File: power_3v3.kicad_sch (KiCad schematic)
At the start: 14 parts, among them U5 LTC3111EDE

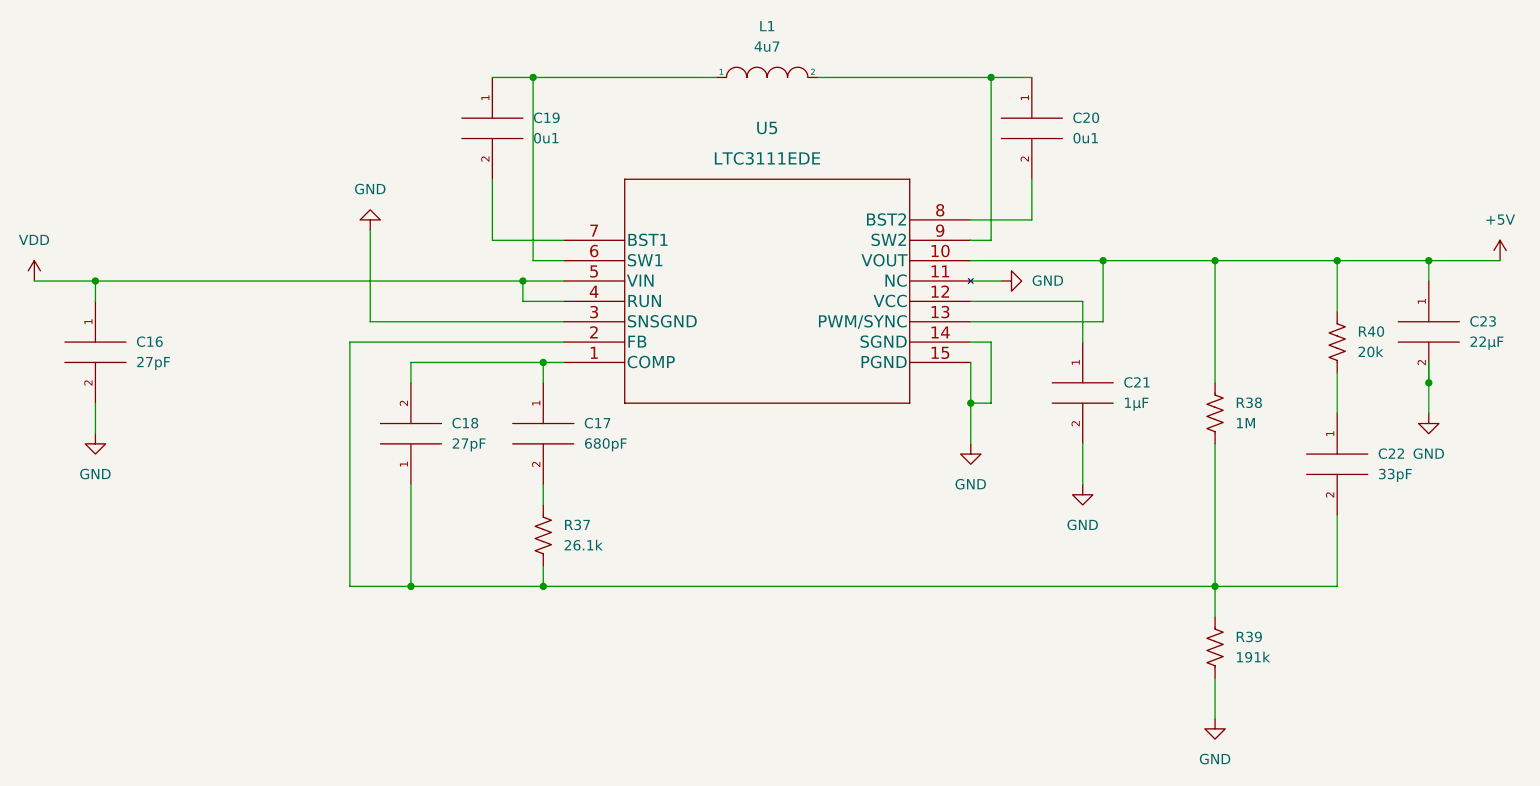
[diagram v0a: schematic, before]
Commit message: Update board design
5v and 3v3 power blocks wired up.
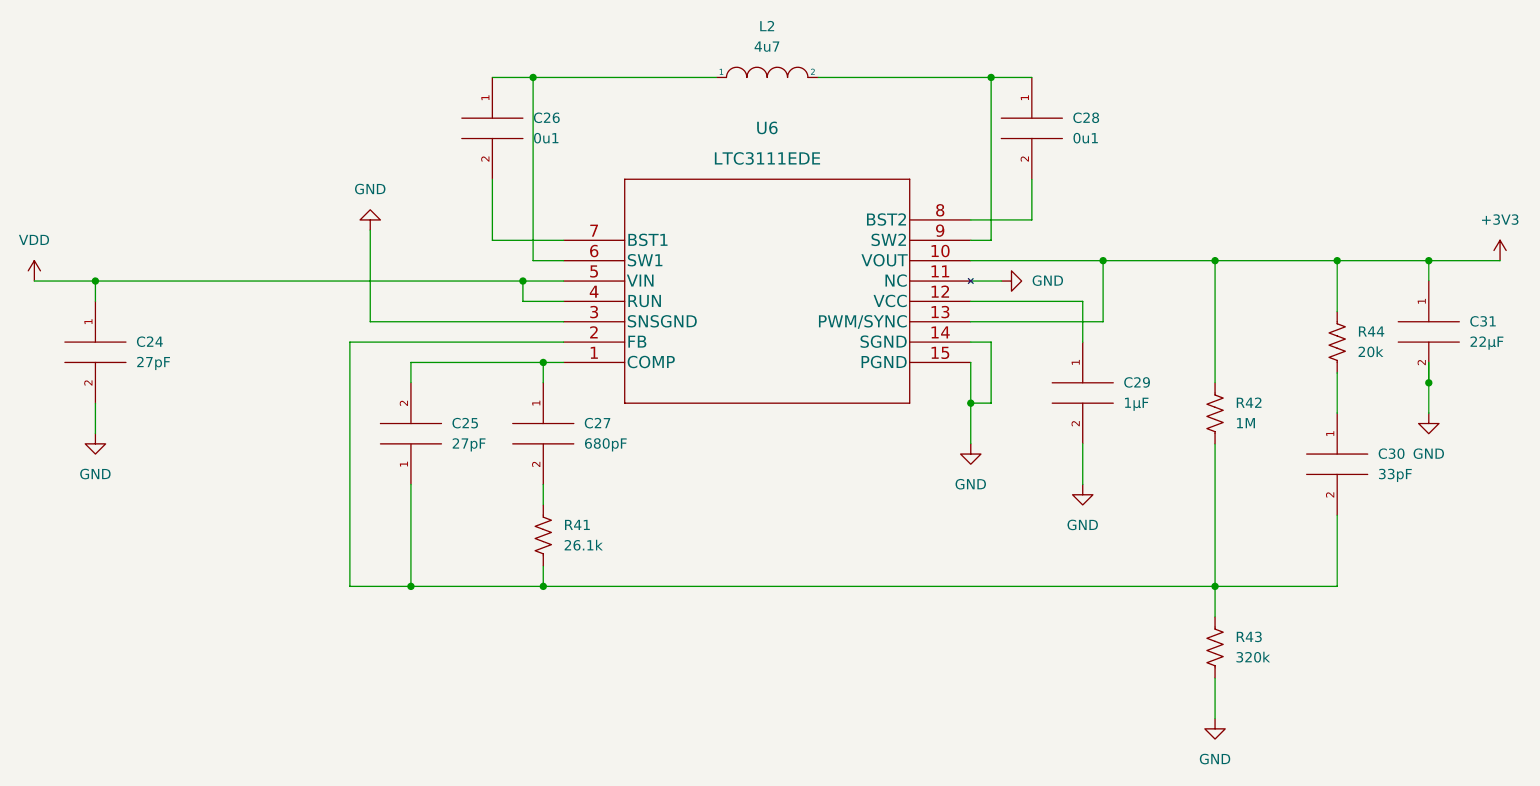
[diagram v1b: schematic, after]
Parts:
- removed C16, C18: 27pF, Capacitor_SMD:C_0201_0603Metric, symbol pspice:C
- removed C17: 680pF, Capacitor_SMD:C_0603_1608Metric, symbol pspice:C
- removed C19, C20: 0u1, Capacitor_SMD:C_0201_0603Metric, symbol pspice:C
- removed C21: 1µF, Capacitor_SMD:C_0201_0603Metric, symbol pspice:C
- removed C22: 33pF, Capacitor_SMD:C_0603_1608Metric, symbol pspice:C
- removed C23: 22µF, Capacitor_SMD:C_1206_3216Metric, symbol pspice:C
- removed L1: 4u7, Inductor_SMD:L_6.3x6.3_H3, symbol pspice:INDUCTOR
- removed R37: 26.1k, Resistor_SMD:R_0201_0603Metric, symbol Device:R_US
- removed R38: 1M, Resistor_SMD:R_0201_0603Metric, symbol Device:R_US
- removed R39: 191k, Resistor_SMD:R_0201_0603Metric, symbol Device:R_US
- removed R40: 20k, Resistor_SMD:R_0201_0603Metric, symbol Device:R_US
- removed U5: LTC3111EDE, Custom:LTC3111EDE-TRPBF, symbol BuckBoost1:LTC3111EDE-PBF
- added C24, C25: 27pF, Capacitor_SMD:C_0201_0603Metric, symbol pspice:C
- added C26, C28: 0u1, Capacitor_SMD:C_0201_0603Metric, symbol pspice:C
- added C27: 680pF, Capacitor_SMD:C_0603_1608Metric, symbol pspice:C
- added C29: 1µF, Capacitor_SMD:C_0201_0603Metric, symbol pspice:C
- added C30: 33pF, Capacitor_SMD:C_0603_1608Metric, symbol pspice:C
- added C31: 22µF, Capacitor_SMD:C_1206_3216Metric, symbol pspice:C
- added L2: 4u7, Inductor_SMD:L_6.3x6.3_H3, symbol pspice:INDUCTOR
- added R41: 26.1k, Resistor_SMD:R_0201_0603Metric, symbol Device:R_US
- added R42: 1M, Resistor_SMD:R_0201_0603Metric, symbol Device:R_US
- added R43: 320k, Resistor_SMD:R_0201_0603Metric, symbol Device:R_US
- added R44: 20k, Resistor_SMD:R_0201_0603Metric, symbol Device:R_US
- added U6: LTC3111EDE, Custom:LTC3111EDE-TRPBF, symbol BuckBoost1:LTC3111EDE-PBF
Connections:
- net GND: now also C24.2, C29.2, C31.2, R43.2, U6.11 (NC), U6.14 (SGND), U6.15 (PGND), U6.3 (SNSGND)
- net VDD: now also C24.1, U6.4 (RUN), U6.5 (VIN)
- new net: C25.2, C27.1, U6.1 (COMP)
- new net: C27.2, R41.1
- new net: C26.1, L2.1, U6.6 (SW1)
- new net: C26.2, U6.7 (BST1)
- new net: C30.1, R44.2
- new net: C29.1, U6.12 (VCC)
- new net: C25.1, C30.2, R41.2, R42.2, R43.1, U6.2 (FB)
- new net: C28.2, U6.8 (BST2)
- new net: C28.1, L2.2, U6.9 (SW2)
- new net +3V3: C31.1, R42.1, R44.1, U6.10 (VOUT), U6.13 (PWM/SYNC)

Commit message: First week after winter break. Changed Power circuit design to use different DC to DC converter Setting correct footprints for the components like resistors and capacitors.
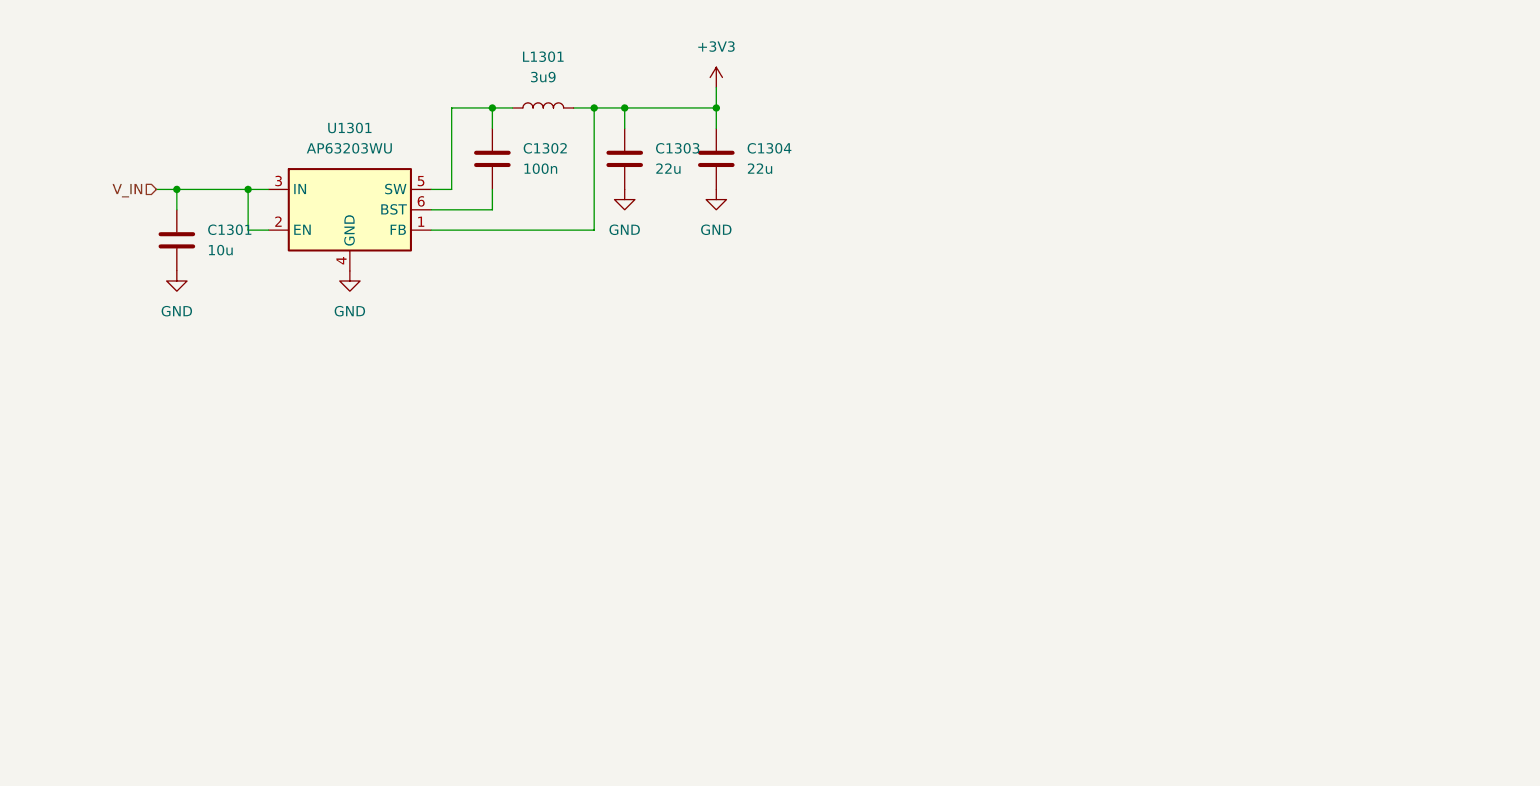
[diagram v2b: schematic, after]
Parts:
- removed C24, C25: 27pF, Capacitor_SMD:C_0201_0603Metric, symbol pspice:C
- removed C26, C28: 0u1, Capacitor_SMD:C_0201_0603Metric, symbol pspice:C
- removed C27: 680pF, Capacitor_SMD:C_0603_1608Metric, symbol pspice:C
- removed C29: 1µF, Capacitor_SMD:C_0201_0603Metric, symbol pspice:C
- removed C30: 33pF, Capacitor_SMD:C_0603_1608Metric, symbol pspice:C
- removed C31: 22µF, Capacitor_SMD:C_1206_3216Metric, symbol pspice:C
- removed L2: 4u7, Inductor_SMD:L_6.3x6.3_H3, symbol pspice:INDUCTOR
- removed R41: 26.1k, Resistor_SMD:R_0201_0603Metric, symbol Device:R_US
- removed R42: 1M, Resistor_SMD:R_0201_0603Metric, symbol Device:R_US
- removed R43: 320k, Resistor_SMD:R_0201_0603Metric, symbol Device:R_US
- removed R44: 20k, Resistor_SMD:R_0201_0603Metric, symbol Device:R_US
- removed U6: LTC3111EDE, Custom:LTC3111EDE-TRPBF, symbol BuckBoost1:LTC3111EDE-PBF
- added C1301: 10u, Capacitor_SMD:C_0603_1608Metric, symbol Device:C
- added C1302: 100n, Capacitor_SMD:C_0805_2012Metric, symbol Device:C
- added C1303, C1304: 22u, Capacitor_SMD:C_0603_1608Metric, symbol Device:C
- added L1301: 3u9, symbol Device:L
- added U1301: AP63203WU, Package_TO_SOT_SMD:TSOT-23-6, symbol Regulator_Switching:AP63203WU
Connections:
- net +3V3: now also C1303.1, C1304.1, L1301.2, U1301.1 (FB)
- net GND: now also C1301.2, C1303.2, C1304.2, U1301.4 (GND)
- new net: C1302.1, L1301.1, U1301.5 (SW)
- new net: C1302.2, U1301.6 (BST)
- new net V_IN: C1301.1, U1301.2 (EN), U1301.3 (IN)

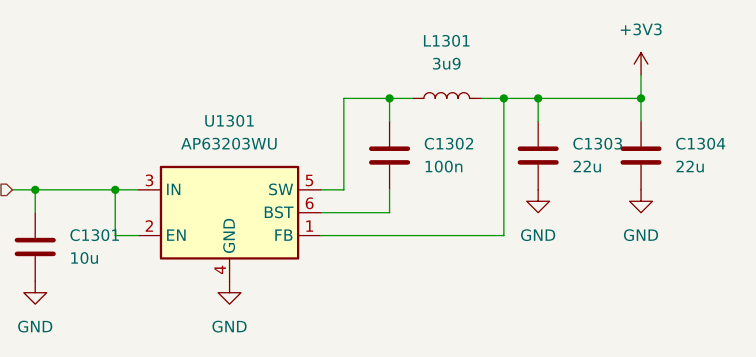
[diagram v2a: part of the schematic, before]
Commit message: Weekend progress
Things that remain:
4 LEDs to Microcontroller
7-Seg to Microcontroller
LCD to Microcontroller
Microphone and Speakers to Microcontroller
Power circuitry
USB-C connector
Reset and Boot buttons
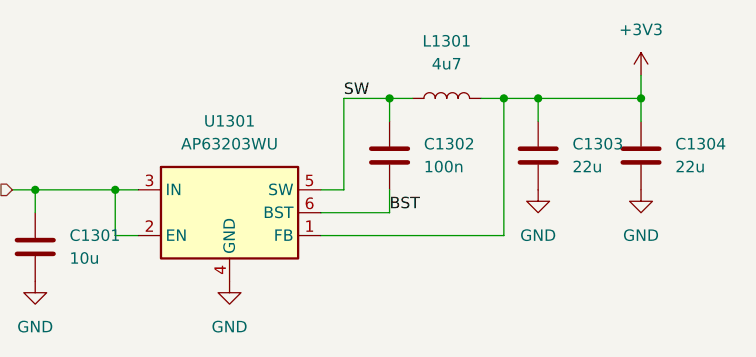
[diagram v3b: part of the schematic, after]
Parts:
- L1301: value 3u9 -> 4u7; footprint (none) -> Inductor_SMD:L_1008_2520Metric; Manufacturer_Name (none) -> Samsung Electro-Mechanics; Manufacturer_Part_Number (none) -> CIGW252010GL4R7MNE
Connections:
- net SW: now reaches C1302.1, L1301.1, U1301.5 (SW)
- net BST: now reaches C1302.2, U1301.6 (BST)
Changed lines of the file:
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@@
     (stroke (width 0) (type default) (color 0 0 0 0))
+  )
+  (label "SW" (at 109.22 58.42 0)
+    (effects (font (size 1.27 1.27)) (justify left bottom))
+  )
+  (label "BST" (at 114.3 71.12 0)
+    (effects (font (size 1.27 1.27)) (justify left bottom))
   )
   (hierarchical_label "V_IN" (shape input) (at 72.39 68.58 180)
@@
     (in_bom yes) (on_board yes) (fields_autoplaced)
     (property "Reference" "L1301" (id 0) (at 120.65 52.07 90))
-    (property "Value" "3u9" (id 1) (at 120.65 54.61 90))
-    (property "Footprint" "" (id 2) (at 120.65 58.42 0)
+    (property "Value" "4u7" (id 1) (at 120.65 54.61 90))
+    (property "Footprint" "Inductor_SMD:L_1008_2520Metric" (id 2) (at 120.65 58.42 0)
       (effects (font (size 1.27 1.27)) hide)
     )
@@
       (effects (font (size 1.27 1.27)) hide)
     )
+    (property "Manufacturer_Name" "Samsung Electro-Mechanics" (id 4) (at 120.65 58.42 0)
+      (effects (font (size 1.27 1.27)) hide)
+    )
+    (property "Manufacturer_Part_Number" "CIGW252010GL4R7MNE" (id 5) (at 120.65 58.42 0)
+      (effects (font (size 1.27 1.27)) hide)
+    )

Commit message: Update BOM and POC files
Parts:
- U1301: Manufacturer_Name (none) -> Diodes Incorporated; Manufacturer_Part_Number (none) -> AP63203WU-7
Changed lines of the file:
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@@
+      (effects (font (size 1.27 1.27)) hide)
+    )
+    (property "Manufacturer_Name" "Diodes Incorporated" (id 4) (at 96.52 71.12 0)
+      (effects (font (size 1.27 1.27)) hide)
+    )
+    (property "Manufacturer_Part_Number" "AP63203WU-7" (id 5) (at 96.52 71.12 0)
       (effects (font (size 1.27 1.27)) hide)
     )
